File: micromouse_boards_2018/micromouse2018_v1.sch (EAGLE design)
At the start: 35 parts

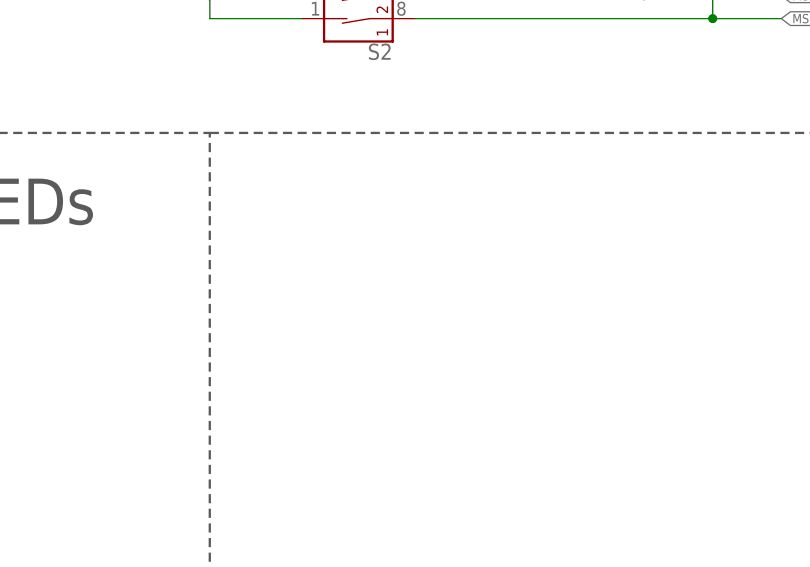
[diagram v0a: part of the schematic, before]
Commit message: Added power switch to schematic
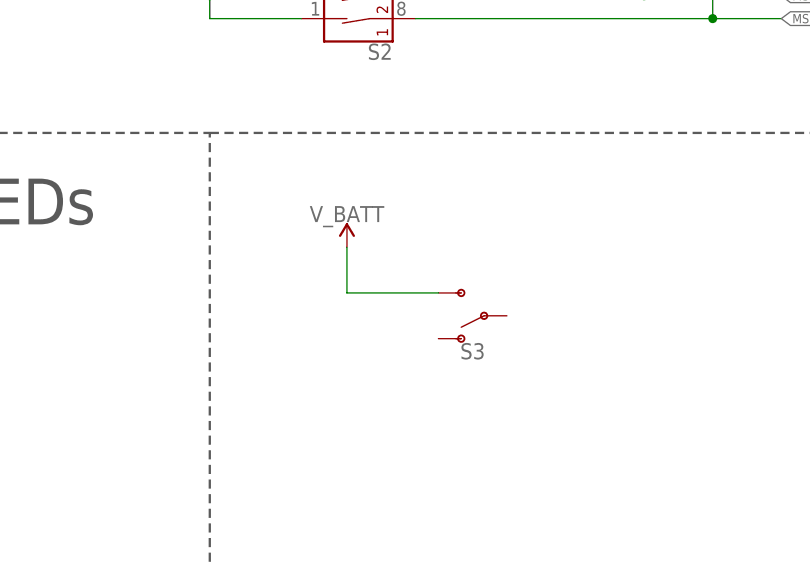
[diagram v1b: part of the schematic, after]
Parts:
- added S3: (no value), SparkFun-Switches:SWITCH-SPDT-PTH-11.6X4.0MM
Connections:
- net V_BATT: now also S3.S
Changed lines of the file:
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@@
 <part name="J3" library="SparkFun-Connectors" deviceset="CONN_03" device="JST-PTH-VERT"/>
 <part name="J4" library="SparkFun-Connectors" deviceset="CONN_03" device="JST-PTH-VERT"/>
+<part name="SUPPLY23" library="SparkFun-PowerSymbols" deviceset="V_BATT" device=""/>
+<part name="S3" library="SparkFun-Switches" deviceset="SWITCH-SPDT" device="-PTH-11.6X4.0MM"/>
 </parts>
 <sheets>
@@
 <instance part="J3" gate="J$1" x="284.48" y="187.96"/>
 <instance part="J4" gate="J$1" x="284.48" y="154.94"/>
+<instance part="SUPPLY23" gate="G$1" x="205.74" y="124.46"/>
+<instance part="S3" gate="1" x="220.98" y="116.84" rot="R180"/>
 </instances>
 <busses>
@@
 <wire x1="129.54" y1="109.22" x2="129.54" y2="116.84" width="0.1524" layer="91"/>
 </segment>
+<segment>
+<pinref part="SUPPLY23" gate="G$1" pin="V_BATT"/>
+<wire x1="205.74" y1="124.46" x2="205.74" y2="119.38" width="0.1524" layer="91"/>
+<wire x1="205.74" y1="119.38" x2="215.9" y2="119.38" width="0.1524" layer="91"/>
+<pinref part="S3" gate="1" pin="S"/>
+</segment>
 </net>

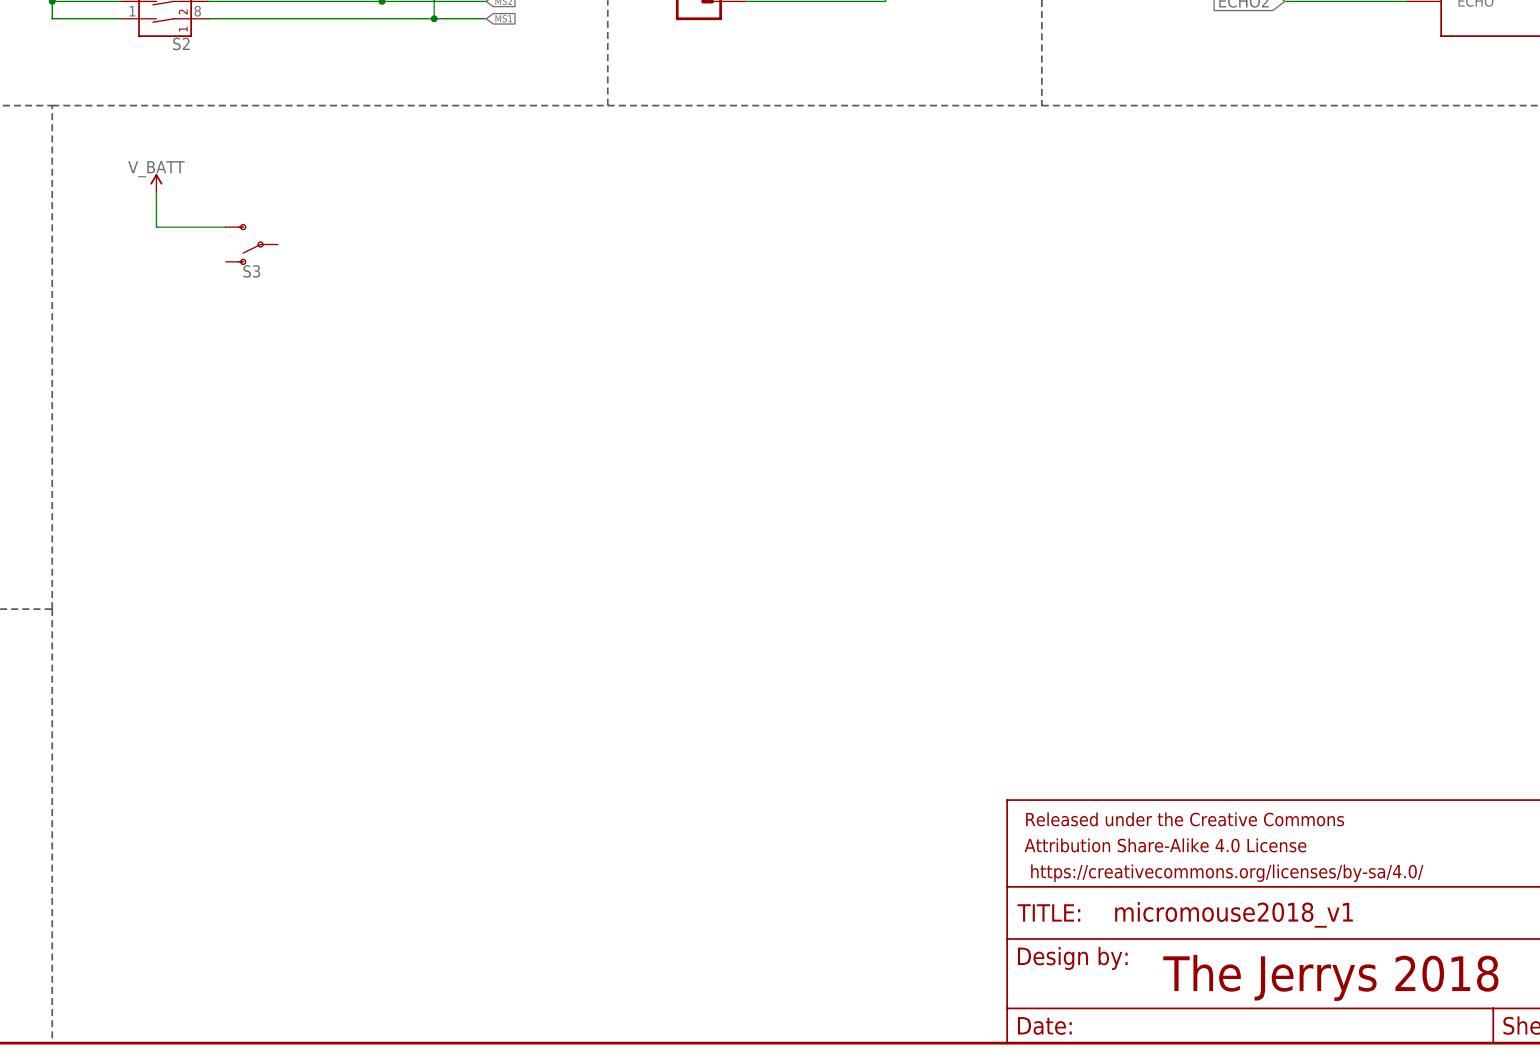
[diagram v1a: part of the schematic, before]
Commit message: Added power circuit
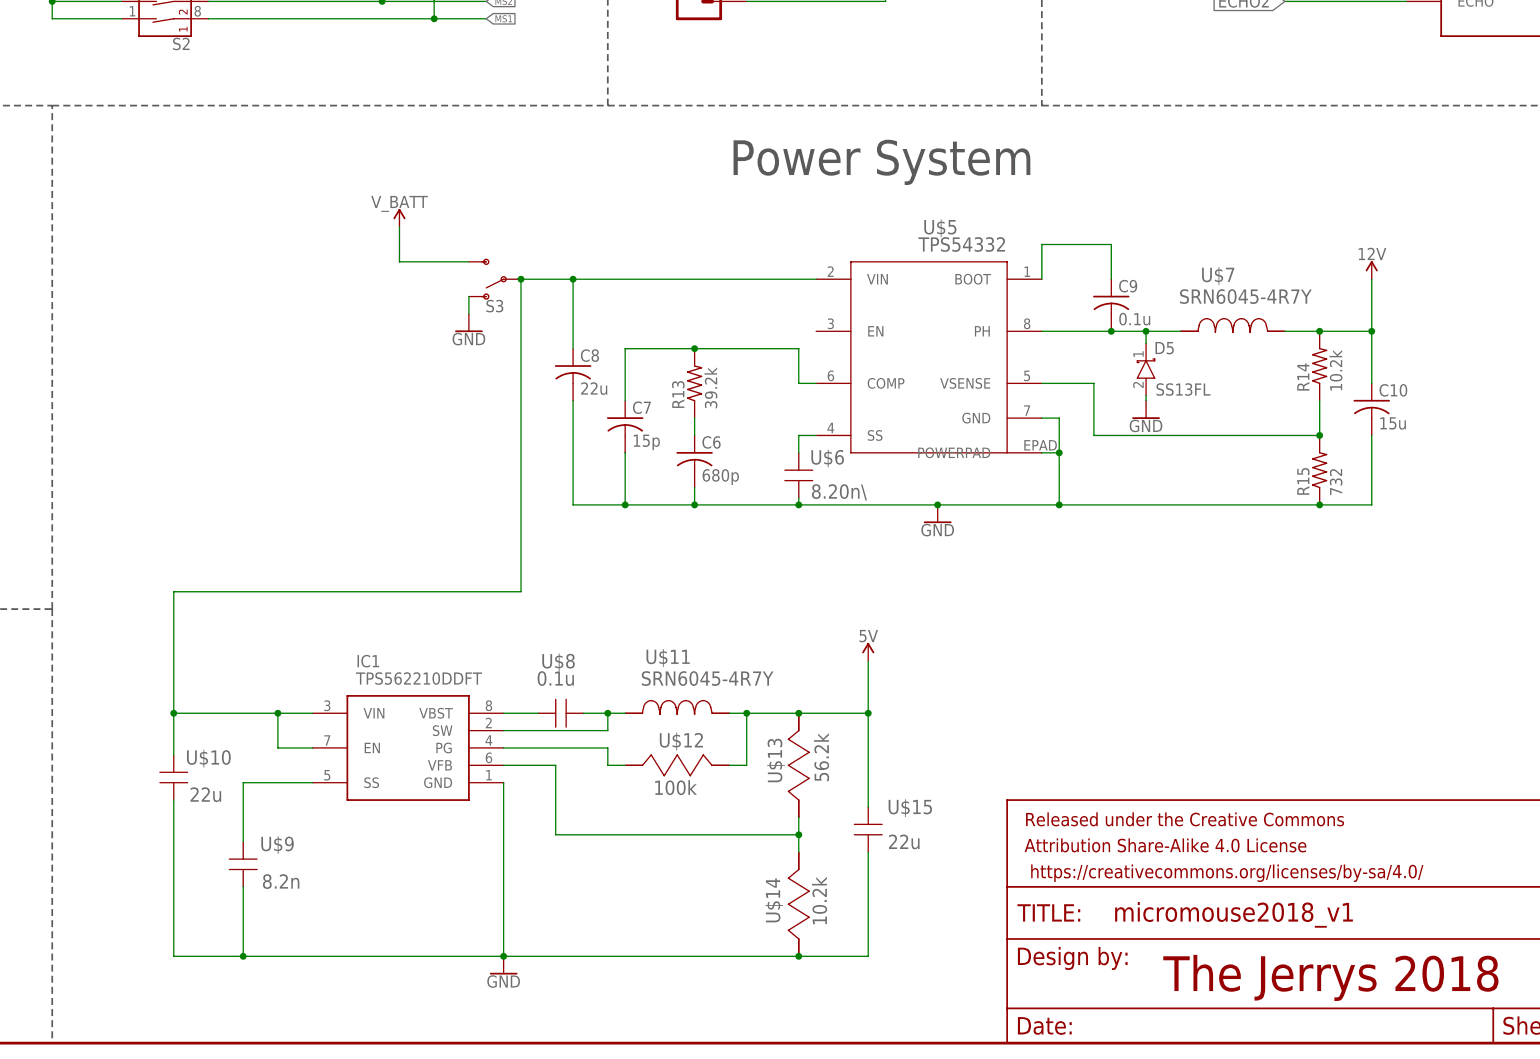
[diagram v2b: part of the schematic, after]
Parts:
- added C10: 15u, resistor:C-USC0805
- added C6: 680p, resistor:C-USC0805
- added C7: 15p, resistor:C-USC0805
- added C8: 22u, rcl:C-USC1210
- added C9: 0.1u, resistor:C-USC0805
- added D5: SS13FL, Scraps:SS13FL
- added IC1: TPS562210DDFT, TPS562210DDFT:TPS562210DDFT
- added R13: 39.2k, resistor:R-US_R0805
- added R14: 10.2k, resistor:R-US_R0805
- added R15: 732, resistor:R-US_R0805
- added U$10: 22u, AcceleratedDesigns_Lib:GRM32ER61E226KE15L
- added U$11, U$7: SRN6045-4R7Y, AcceleratedDesigns_Lib:SRN6045-4R7Y
- added U$12: 100k, AcceleratedDesigns_Lib:RR1220P-104-D
- added U$13: 56.2k, AcceleratedDesigns_Lib:ERJ-6ENF5622V
- added U$14: 10.2k, AcceleratedDesigns_Lib:ERJ-6ENF1022V
- added U$15: 22u, AcceleratedDesigns_Lib:GRM31CR61A226KE19L
- added U$5: TPS54332, TPS54332:TPS54332
- added U$6: 8.20n\, AcceleratedDesigns_Lib:12063A822JAT2A
- added U$8: 0.1u, AcceleratedDesigns_Lib:08053C104KAT2A
- added U$9: 8.2n, AcceleratedDesigns_Lib:12063A822JAT2A
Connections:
- new net N$10: C9.1, U$5.BOOT
- new net N$11: C7.1, R13.2, U$5.COMP
- new net N$12: C6.1, R13.1
- new net N$15: IC1.PG, U$12.2
- new net N$16: IC1.VFB, U$13.2, U$14.1
- new net N$18: IC1.SS, U$9.1
- new net N$19: C8.1, IC1.EN, IC1.VIN, S3.P, U$10.1, U$5.VIN
- new net N$5: U$5.SS, U$6.2
- new net N$6: IC1.VBST, U$8.2
- new net N$7: C9.2, D5.K, U$5.PH, U$7.1
- new net N$8: IC1.SW, U$11.1, U$8.1
- new net N$9: R14.1, R15.2, U$5.VSENSE
- net 12V: now also C10.1, R14.2, U$7.2
- net 5V: now also U$11.2, U$12.1, U$13.1, U$15.1
- net GND: now also C10.2, C6.2, C7.2, C8.2, D5.A, IC1.GND, R15.1, S3.O, U$10.2, U$14.2, U$15.2, U$5.GND, U$5.POWERPAD, U$6.1, U$9.2
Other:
- note added: "Power System"
- moved on the sheet: S3

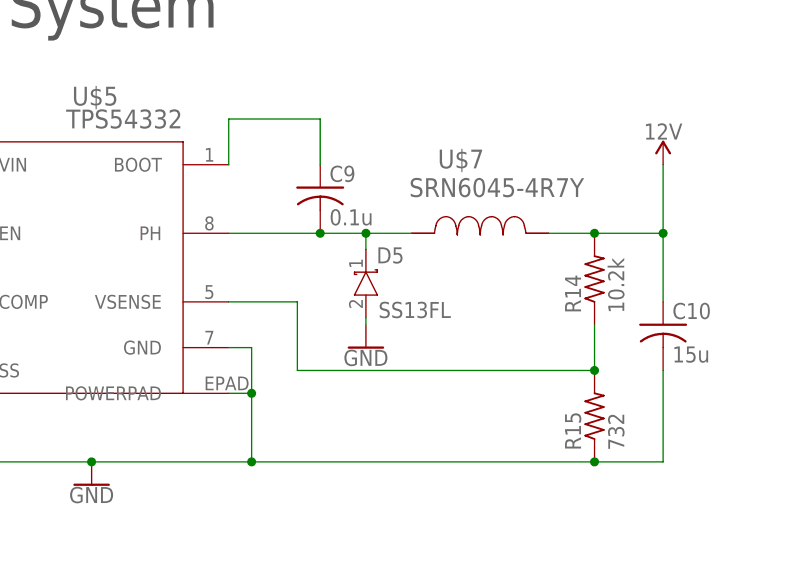
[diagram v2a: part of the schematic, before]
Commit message: Changed SS31FL diode to CMS06 for better heat dissipation
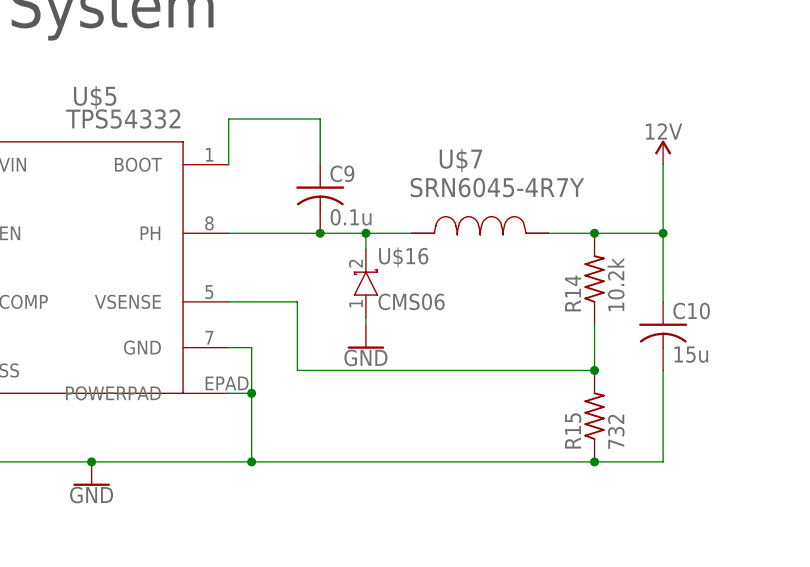
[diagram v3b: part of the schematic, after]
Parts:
- removed D5: SS13FL, Scraps:SS13FL
- added U$16: CMS06, Scraps:CMS06
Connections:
- net GND: now also U$16.A; no longer D5.A
- net N$7: now also U$16.K; no longer D5.K
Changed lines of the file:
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@@
 <part name="C9" library="resistor" library_urn="urn:adsk.eagle:library:348" deviceset="C-US" device="C0805" package3d_urn="urn:adsk.eagle:package:26137/1" value="0.1u"/>
 <part name="C10" library="resistor" library_urn="urn:adsk.eagle:library:348" deviceset="C-US" device="C0805" package3d_urn="urn:adsk.eagle:package:26137/1" value="15u"/>
-<part name="D5" library="Scraps" deviceset="SS13FL" device=""/>
 <part name="R14" library="resistor" library_urn="urn:adsk.eagle:library:348" deviceset="R-US_" device="R0805" package3d_urn="urn:adsk.eagle:package:26059/1" value="10.2k"/>
 <part name="R15" library="resistor" library_urn="urn:adsk.eagle:library:348" deviceset="R-US_" device="R0805" package3d_urn="urn:adsk.eagle:package:26059/1" value="732"/>
@@
 <part name="GND19" library="SparkFun-PowerSymbols" deviceset="GND" device=""/>
 <part name="GND20" library="SparkFun-PowerSymbols" deviceset="GND" device=""/>
+<part name="U$16" library="Scraps" deviceset="CMS06" device=""/>
 </parts>
 <sheets>
@@
 <instance part="C9" gate="G$1" x="345.44" y="109.22"/>
 <instance part="C10" gate="G$1" x="383.54" y="93.98"/>
-<instance part="D5" gate="G$1" x="350.52" y="99.06" smashed="yes" rot="R270">
-<attribute name="NAME" x="351.69" y="101.69" size="1.778" layer="95" align="center-left"/>
-<attribute name="VALUE" x="351.9" y="95.62" size="1.778" layer="96" align="center-left"/>
-</instance>
 <instance part="R14" gate="G$1" x="375.92" y="99.06" rot="R90"/>
 <instance part="R15" gate="G$1" x="375.92" y="83.82" rot="R90"/>
@@
 <instance part="GND19" gate="1" x="256.54" y="10.16"/>
 <instance part="GND20" gate="1" x="251.46" y="104.14"/>
+<instance part="U$16" gate="G$1" x="350.52" y="99.06" smashed="yes" rot="R270">
+<attribute name="NAME" x="351.79" y="101.6" size="1.778" layer="95" align="center-left"/>
+<attribute name="VALUE" x="351.79" y="96.52" size="1.778" layer="96" align="center-left"/>
+</instance>
 </instances>
 <busses>
@@
 <pinref part="GND14" gate="1" pin="GND"/>
 <pinref part="J4" gate="J$1" pin="2"/>
-</segment>
-<segment>
-<pinref part="D5" gate="G$1" pin="A"/>
-<pinref part="GND16" gate="1" pin="GND"/>
-<wire x1="350.52" y1="94.742" x2="350.52" y2="93.98" width="0.1524" layer="91"/>
 </segment>
 <segment>
@@
 <pinref part="GND20" gate="1" pin="GND"/>
 </segment>
+<segment>
+<pinref part="GND16" gate="1" pin="GND"/>
+<pinref part="U$16" gate="G$1" pin="A"/>
+<wire x1="350.52" y1="93.98" x2="350.52" y2="94.742" width="0.1524" layer="91"/>
+</segment>
 </net>
 <net name="ENABLE1" class="0">
@@
 <wire x1="335.28" y1="104.14" x2="345.44" y2="104.14" width="0.1524" layer="91"/>
 <pinref part="U$7" gate="A" pin="1"/>
+<junction x="345.44" y="104.14"/>
 <wire x1="345.44" y1="104.14" x2="350.52" y2="104.14" width="0.1524" layer="91"/>
-<junction x="345.44" y="104.14"/>
-<pinref part="D5" gate="G$1" pin="K"/>
+<pinref part="U$16" gate="G$1" pin="K"/>
 <wire x1="350.52" y1="104.14" x2="355.6" y2="104.14" width="0.1524" layer="91"/>
 <wire x1="350.52" y1="102.362" x2="350.52" y2="104.14" width="0.1524" layer="91"/>

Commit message: Rough draft for 5V power circuit layout
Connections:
- net N$19 renamed VIN
- net N$8 renamed BOOT
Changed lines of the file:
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@@
 </segment>
 </net>
-<net name="N$8" class="0">
+<net name="BOOT" class="0">
 <segment>
 <pinref part="U$8" gate="A" pin="1"/>
@@
 </segment>
 </net>
-<net name="N$19" class="0">
+<net name="VIN" class="0">
 <segment>
 <pinref part="IC1" gate="G$1" pin="VIN"/>
